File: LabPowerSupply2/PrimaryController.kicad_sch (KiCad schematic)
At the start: 33 parts, among them Y1 8M

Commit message: Updated Version 2
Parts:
- removed R_I2C1, R_I2C2: 4.7k, Resistor_SMD:R_0603_1608Metric, symbol Device:R_US
- added R1_I2C1, R2_I2C1: 4.7k, Resistor_SMD:R_0603_1608Metric, symbol Device:R_US
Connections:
- net 3.3 Volts: now also R1_I2C1.1, R2_I2C1.2
- net I2C SCL: now also MCU_1.58 (PB6), R2_I2C1.1; no longer MCU_1.59 (PB7)
- net I2C SDA: now also MCU_1.59 (PB7), R1_I2C1.2; no longer MCU_1.58 (PB6)

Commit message: Beautifing the Schematic
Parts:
- removed A1_1, D1_1, D2_1: Conn_01x01_Male, symbol Connector:Conn_01x01_Male
- removed ADC342_1: Conn_01x03_Male, Connector_PinHeader_2.54mm:PinHeader_1x03_P2.54mm_Vertical, symbol Connector:Conn_01x03_Male
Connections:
- net 3.3 Volts: now also R1_Boot1.1; no longer R1_Boot1.2
- net GND: no longer R2_Boot1.2
- net at J_Boot1.1 (Pin_1): now also R1_Boot1.2; no longer R1_Boot1.1
- net at J_Boot1.3 (Pin_3): now also R2_Boot1.2; no longer R2_Boot1.1
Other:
- moved on the sheet: J_Boot1, R1_Boot1, R2_Boot1, R_Reset1, SW_Reset1

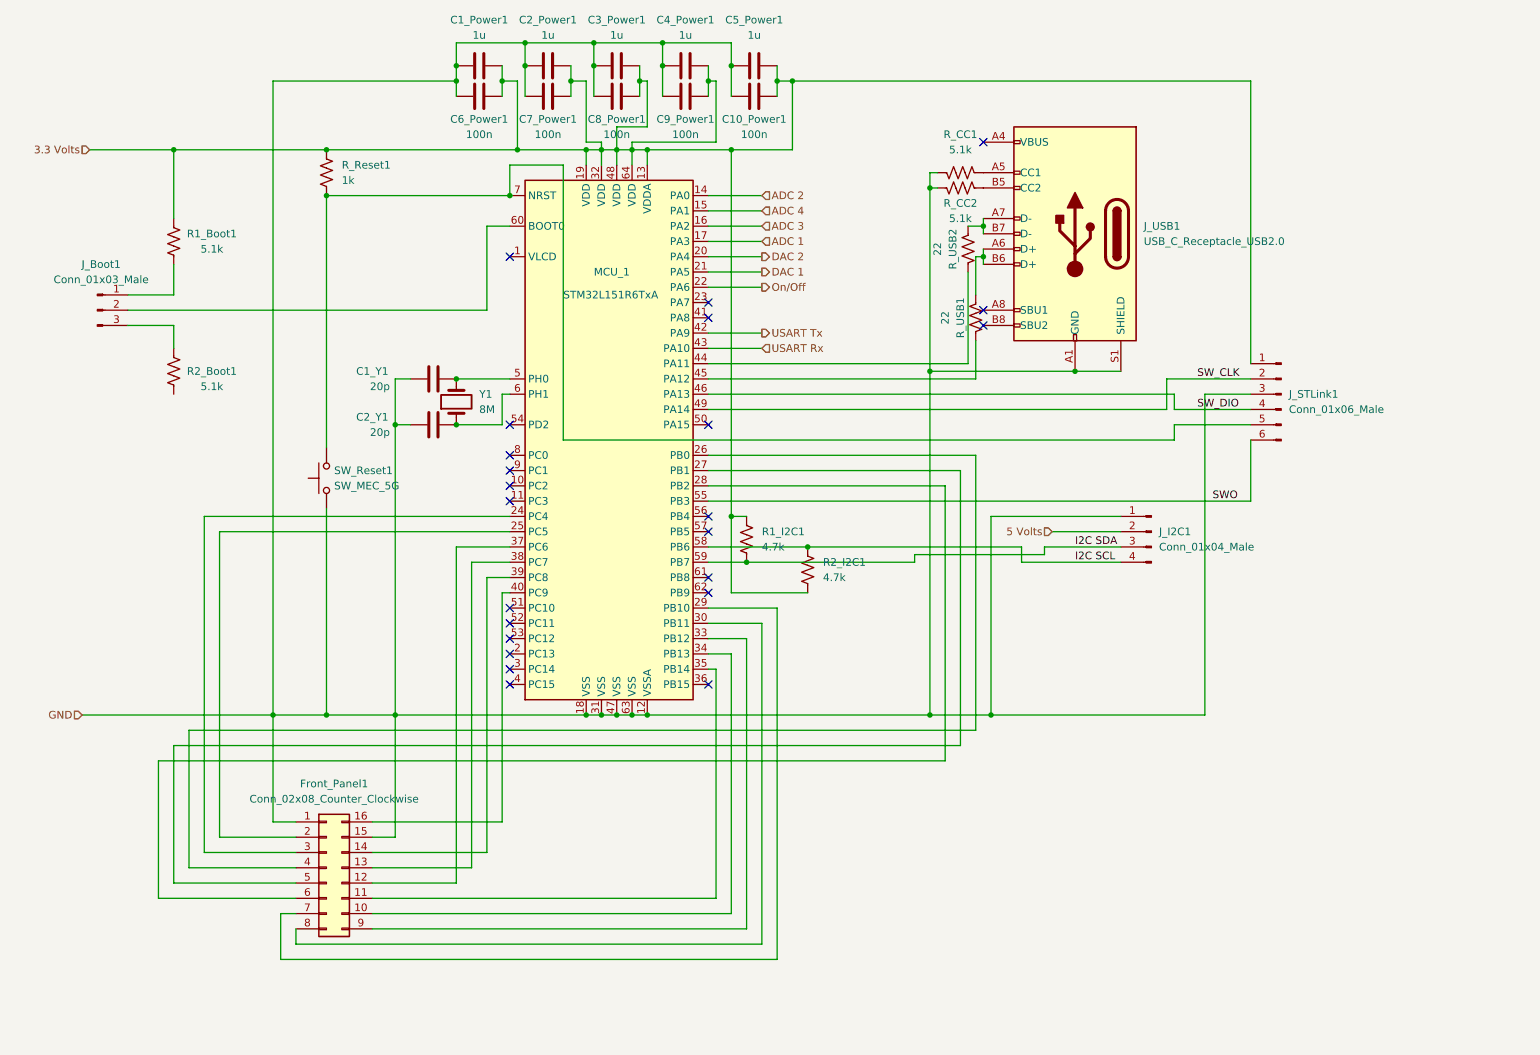
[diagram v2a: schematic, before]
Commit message: Fixed the Beautified Schematics
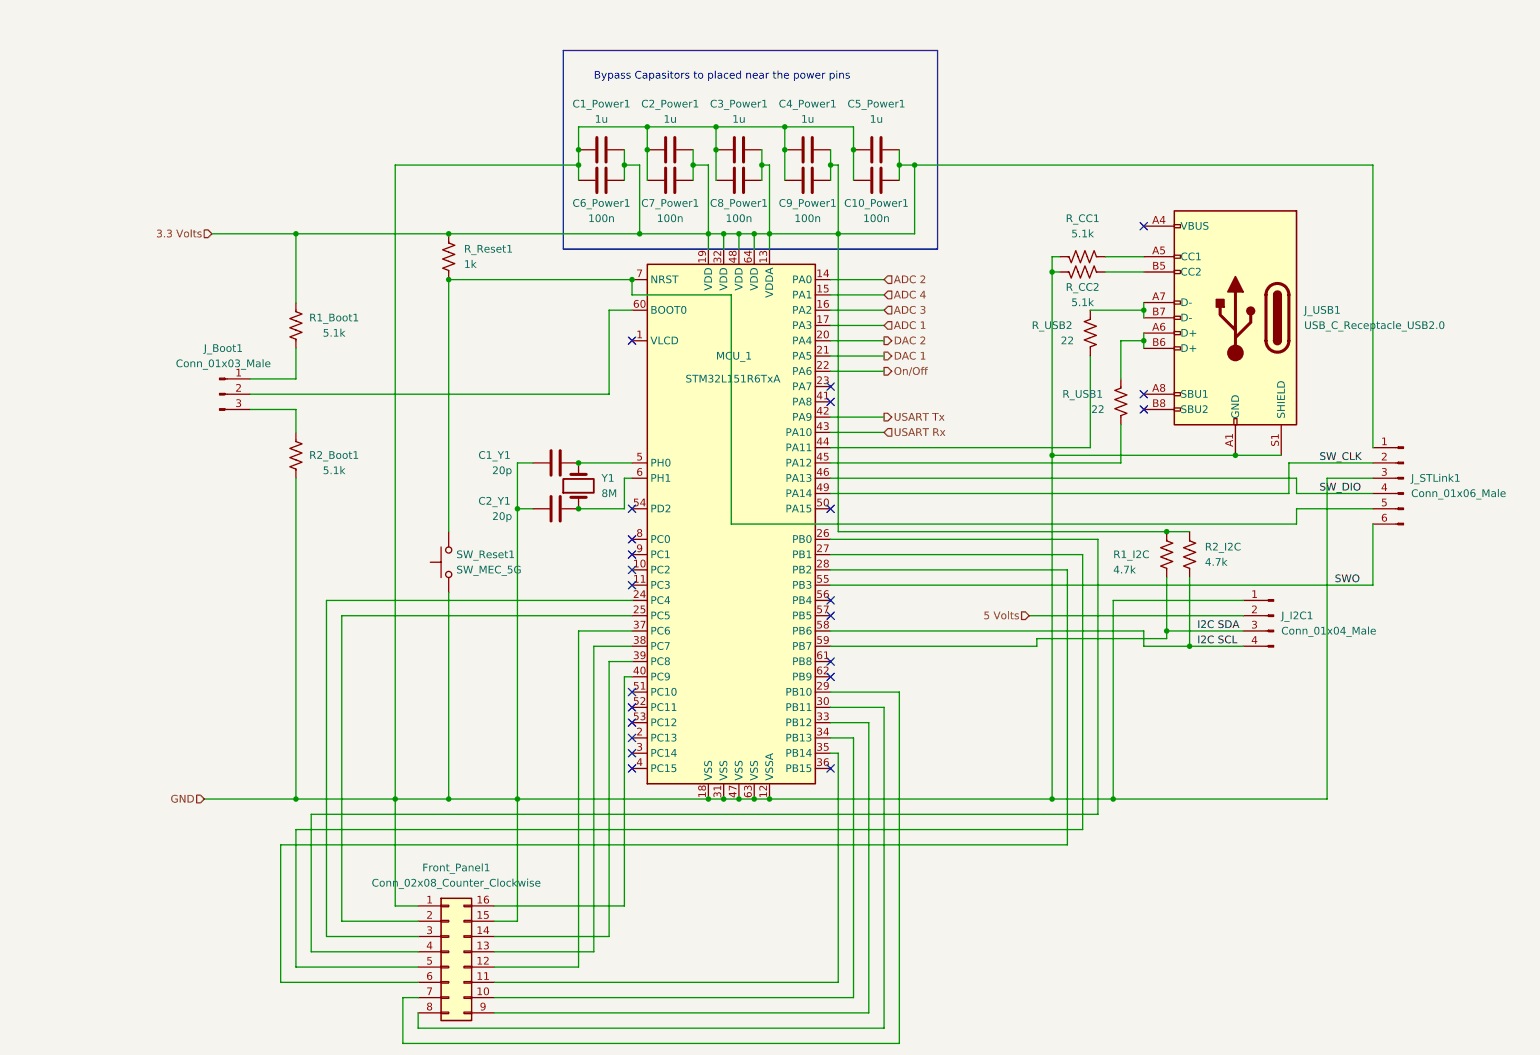
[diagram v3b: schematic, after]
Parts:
- removed R1_I2C1, R2_I2C1: 4.7k, Resistor_SMD:R_0603_1608Metric, symbol Device:R_US
- added R1_I2C, R2_I2C: 4.7k, Resistor_SMD:R_0603_1608Metric, symbol Device:R_US
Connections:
- net 3.3 Volts: now also R1_I2C.2, R2_I2C.1
- net GND: now also R2_Boot1.1
- net I2C SCL: now also R2_I2C.2
- net I2C SDA: now also R1_I2C.1
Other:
- note added: "Bypass Capasitors to placed near the power pins"
- moved on the sheet: C10_Power1, C1_Power1, C1_Y1, C2_Power1, C2_Y1, C3_Power1, C4_Power1, C5_Power1, C6_Power1, C7_Power1, C8_Power1, C9_Power1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

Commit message: Getting new code
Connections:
- net SWO renamed SW_O
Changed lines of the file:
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@@
     (effects (font (size 1.27 1.27)) (justify left bottom))
   )
-  (label "SWO" (at 240.03 109.22 0)
+  (label "SW_O" (at 240.03 109.22 0)
     (effects (font (size 1.27 1.27)) (justify left bottom))
   )

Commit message: Changed symbols to actual MOSFETs
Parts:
- renumbered R1_I2C to R1_I2C1, R2_I2C to R2_I2C1
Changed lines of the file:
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@@
   (symbol (lib_id "Device:R_US") (at 212.09 104.14 180) (unit 1)
     (in_bom yes) (on_board yes)
-    (property "Reference" "R1_I2C" (id 0) (at 203.2 104.14 0)
+    (property "Reference" "R1_I2C1" (id 0) (at 203.2 104.14 0)
       (effects (font (size 1.27 1.27)) (justify right))
     )
@@
   (symbol (lib_id "Device:R_US") (at 215.9 104.14 0) (unit 1)
     (in_bom yes) (on_board yes) (fields_autoplaced)
-    (property "Reference" "R2_I2C" (id 0) (at 218.44 102.8699 0)
+    (property "Reference" "R2_I2C1" (id 0) (at 218.44 102.8699 0)
       (effects (font (size 1.27 1.27)) (justify left))
     )
